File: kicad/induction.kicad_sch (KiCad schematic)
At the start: 22 parts, among them Q2 NPN, T1 Transformer_1P_1S, T2 Transformer_1P_1S

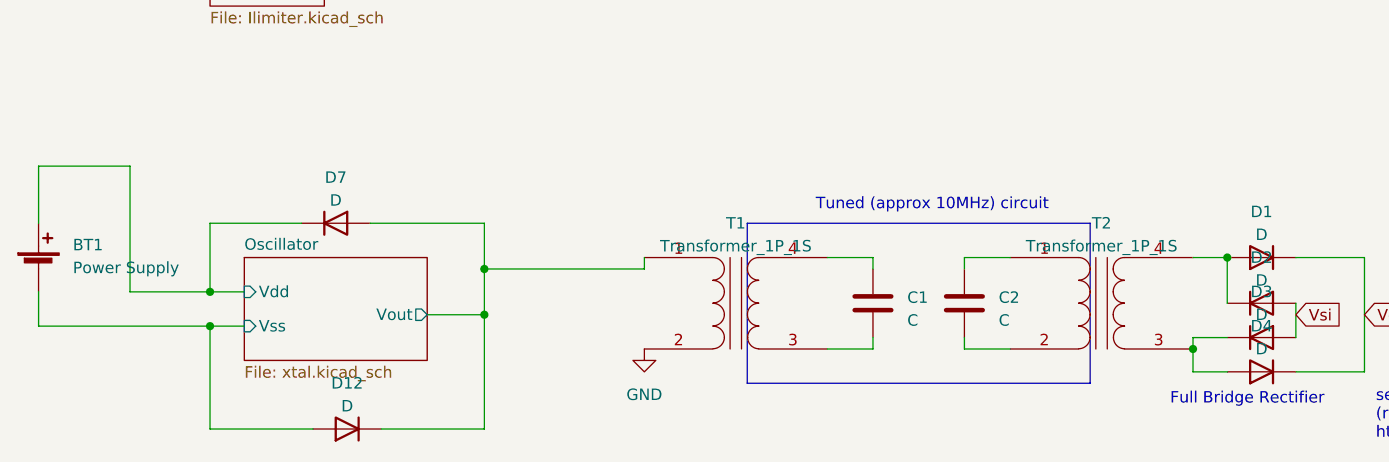
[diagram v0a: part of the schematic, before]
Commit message: Add inverter driver
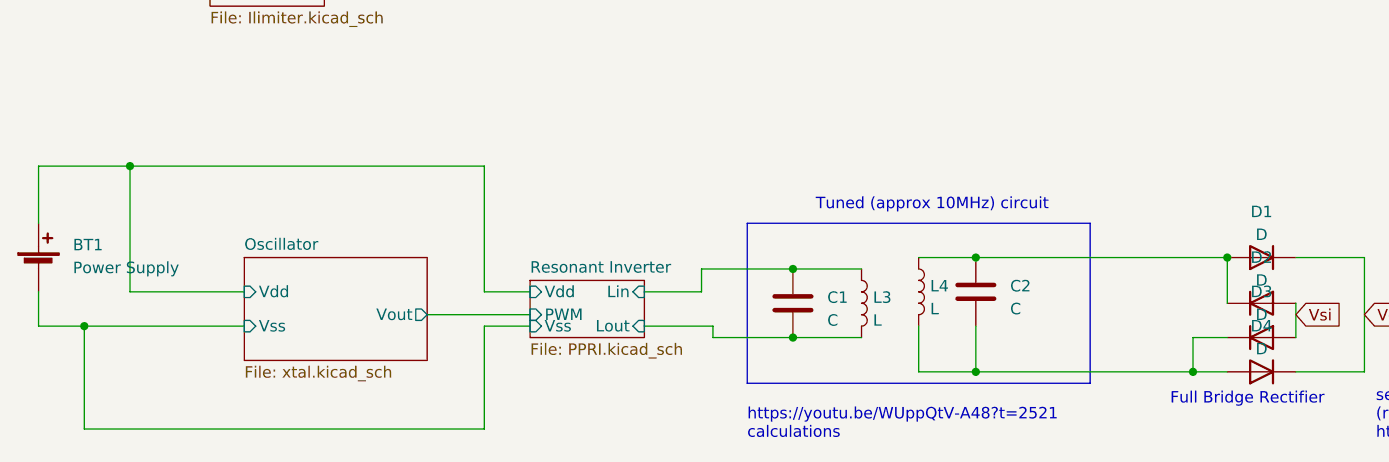
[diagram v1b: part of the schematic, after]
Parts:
- removed D12, D7: D, symbol Device:D
- removed T1, T2: Transformer_1P_1S, symbol Device:Transformer_1P_1S
- added L3, L4: L, symbol Device:L
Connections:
- net at D3.1 (K), D4.2 (A): now also C2.2, L4.2
- net at D1.2 (A), D2.1 (K): now also C2.1, L4.1
- net Resonant Inverter/Lout: now reaches C1.2
- net Resonant Inverter/Lout: now also L3.2
- net Resonant Inverter/Lin: now reaches C1.1
- net Resonant Inverter/Lin: now also L3.1
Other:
- added sheet Resonant Inverter (PPRI.kicad_sch)
- note added: "https://youtu.be/WUppQtV-A48?t=2521 calculations"
